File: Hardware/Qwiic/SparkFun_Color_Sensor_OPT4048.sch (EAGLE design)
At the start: 28 parts, among them J1 QWIIC_RIGHT_ANGLE, J2 QWIIC_RIGHT_ANGLE, U1 OPT4048

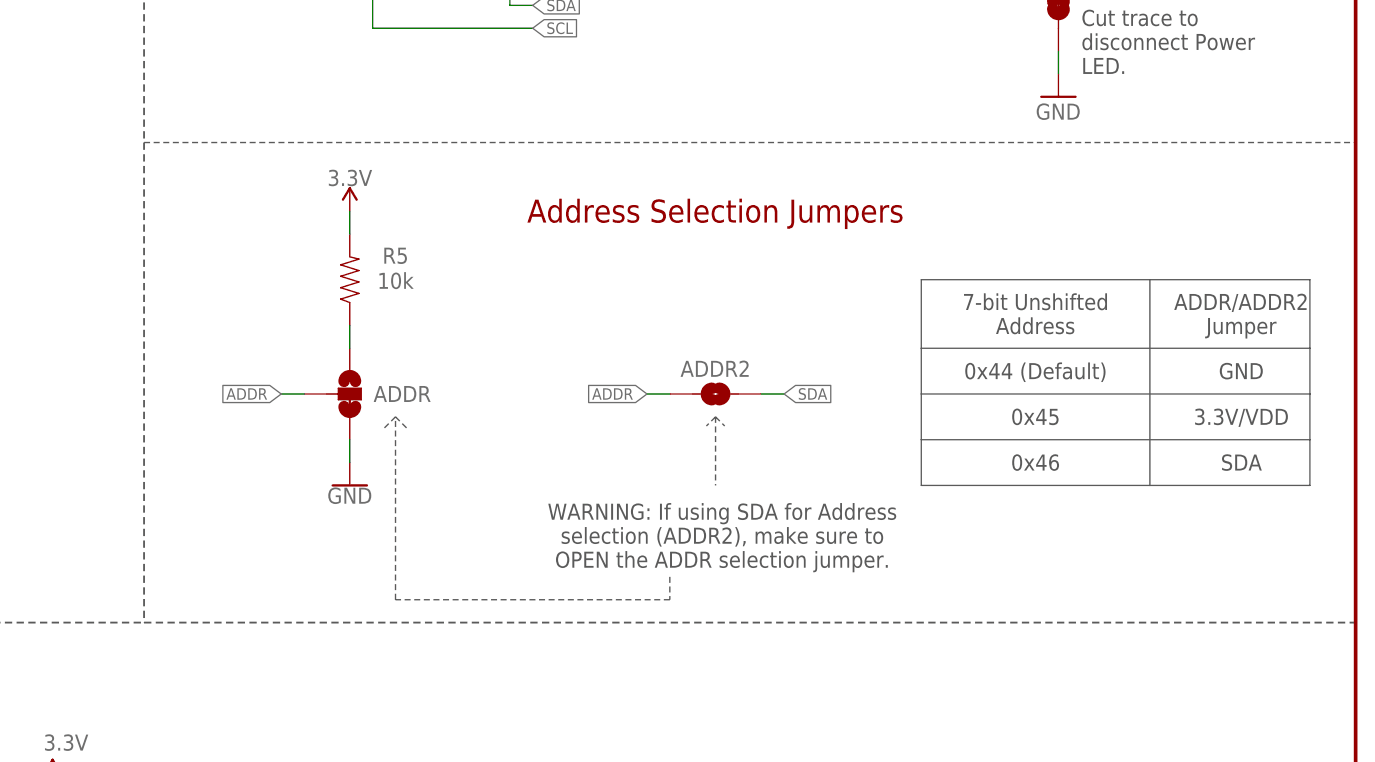
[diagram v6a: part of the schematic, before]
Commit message: Changes Jumper selection, moves resistors away from IC, and changes decoupling cap to smaller package
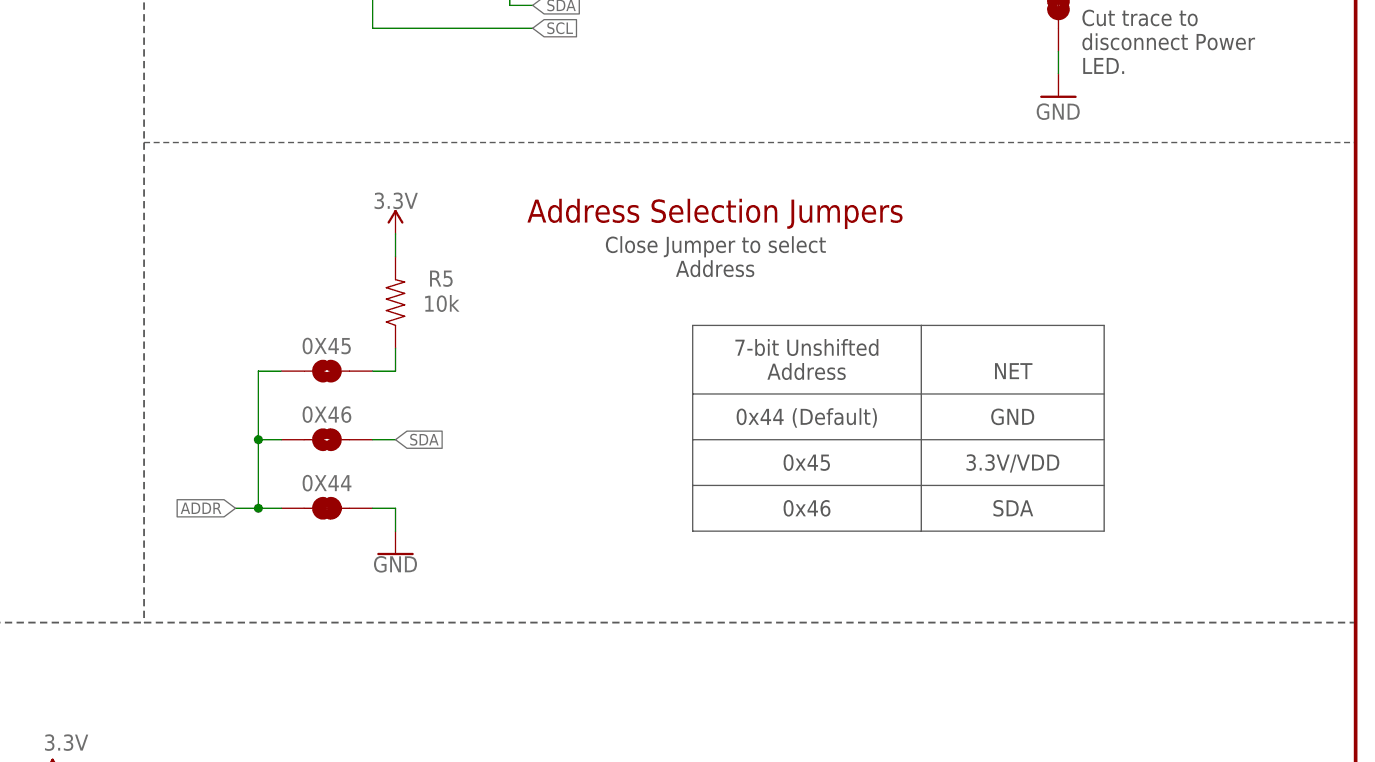
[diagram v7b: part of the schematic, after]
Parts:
- removed ADDR: JUMPER-SMT_3_1-NC_TRACE_SILK, SparkFun-Jumpers:JUMPER-SMT_3_1-NC_TRACE_SILK
- removed ADDR2: JUMPER-SMT_2_NO_SILK, SparkFun-Jumpers:JUMPER-SMT_2_NO_SILK
- added 0X44: JUMPER-SMT_2_NC_TRACE_SILK, SparkFun-Jumpers:JUMPER-SMT_2_NC_TRACE_SILK
- added 0X45, 0X46: JUMPER-SMT_2_NO_SILK, SparkFun-Jumpers:JUMPER-SMT_2_NO_SILK
- C1: device SparkFun-Capacitors:0.1UF-0603-25V-(+80/-20%) -> SparkFun-Capacitors:0.1UF-0402T-16V-10%
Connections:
- removed net N$1: ADDR.1, R5.1
- new net N$4: 0X45.2, R5.1
- net ADDR: now also 0X44.1, 0X45.1, 0X46.1; no longer ADDR.2, ADDR2.1
- net GND: now also 0X44.2; no longer ADDR.3
- net SDA: now also 0X46.2; no longer ADDR2.2
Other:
- note added: "Close Jumper to select Address"
- note added: "NET"
- note removed: "ADDR/ADDR2 Jumper"
- note removed: "WARNING: If using SDA for Address selection (ADDR2), make sure to OPEN the ADDR selection jumper."
- moved on the sheet: R5

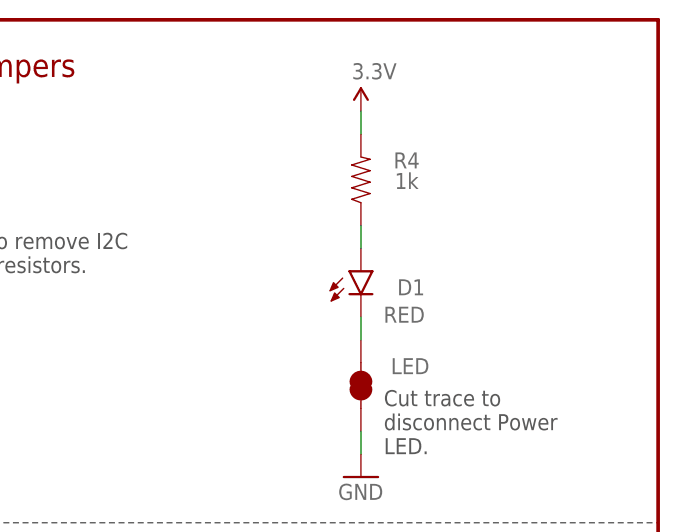
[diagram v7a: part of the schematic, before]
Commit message: Adds correct red LEDs and their resistors, updates PROD_ID for part.
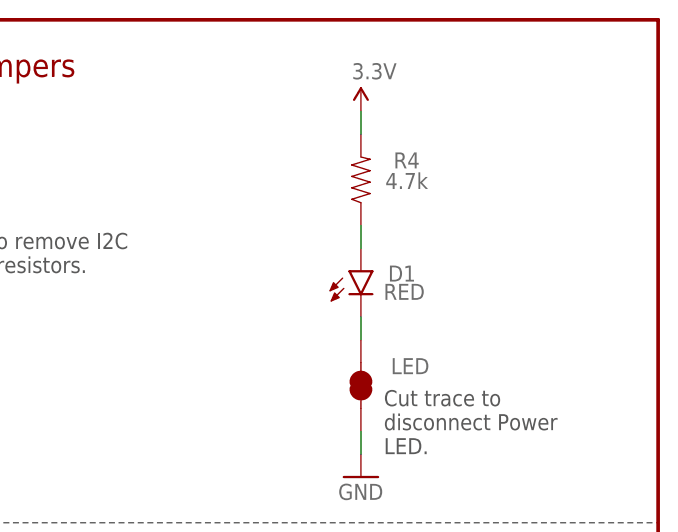
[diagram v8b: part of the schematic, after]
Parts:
- D1: device SparkFun-LED:LED-RED0603 -> SparkFun-LED:LED-RED_0603-KB
- R4: value 1k -> 4.7k; device SparkFun-Resistors:1KOHM-0603-1/10W-1% -> SparkFun-Resistors:4.7KOHM-0603-1/10W-1%
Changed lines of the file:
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@@
 <part name="GND3" library="SparkFun-PowerSymbols" deviceset="GND" device=""/>
 <part name="J2" library="SparkFun-Connectors" deviceset="QWIIC_CONNECTOR" device="JS-1MM" value="QWIIC_RIGHT_ANGLE"/>
-<part name="D1" library="SparkFun-LED" deviceset="LED-RED" device="0603" value="RED"/>
-<part name="R4" library="SparkFun-Resistors" deviceset="1KOHM" device="-0603-1/10W-1%" value="1k"/>
+<part name="D1" library="SparkFun-LED" deviceset="LED-RED" device="_0603-KB" value="RED"/>
+<part name="R4" library="SparkFun-Resistors" deviceset="4.7KOHM" device="-0603-1/10W-1%" value="4.7k"/>
 <part name="LED" library="SparkFun-Jumpers" deviceset="JUMPER-SMT_2_NC_TRACE" device="_SILK" package3d_urn="urn:adsk.eagle:package:39281/1"/>
 <part name="SUPPLY3" library="SparkFun-PowerSymbols" deviceset="3.3V" device=""/>
@@
 </instance>
 <instance part="D1" gate="G$1" x="215.9" y="157.48" smashed="yes">
-<attribute name="NAME" x="223.012" y="156.591" size="1.778" layer="95" font="vector" rot="R180"/>
-<attribute name="VALUE" x="223.012" y="151.765" size="1.778" layer="96" font="vector" rot="R180" align="top-left"/>
+<attribute name="NAME" x="221.996" y="158.115" size="1.778" layer="95" font="vector" rot="R180"/>
+<attribute name="VALUE" x="223.012" y="154.305" size="1.778" layer="96" font="vector" rot="R180" align="top-left"/>
 </instance>
 <instance part="R4" gate="G$1" x="215.9" y="167.64" smashed="yes" rot="R90">
@@
 <segment>
 <pinref part="U1" gate="G$1" pin="SCL"/>
-<wire x1="71.12" y1="124.46" x2="66.04" y2="124.46" width="0.127" layer="91"/>
+<wire x1="71.12" y1="124.46" x2="66.04" y2="124.46" width="0.1524" layer="91"/>
 <label x="71.12" y="124.46" size="1.27" layer="95" font="vector" xref="yes"/>
 </segment>
@@
 <segment>
 <pinref part="U1" gate="G$1" pin="SDA"/>
-<wire x1="71.12" y1="127" x2="66.04" y2="127" width="0.127" layer="91"/>
+<wire x1="71.12" y1="127" x2="66.04" y2="127" width="0.1524" layer="91"/>
 <label x="71.12" y="127" size="1.27" layer="95" font="vector" xref="yes"/>
 </segment>
